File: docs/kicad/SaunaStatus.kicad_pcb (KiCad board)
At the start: 2 copper layers, 9 parts, among them J1 PT1000-Connector, J2 28BYJ-48, J3 28BYJ-48, U1 ESP32-WROOM-32, U2 MAX31865xAP, U3 DHT21/AM2301, U4 DHT21/AM2301, U5 ULN2003A, U6 ULN2003A

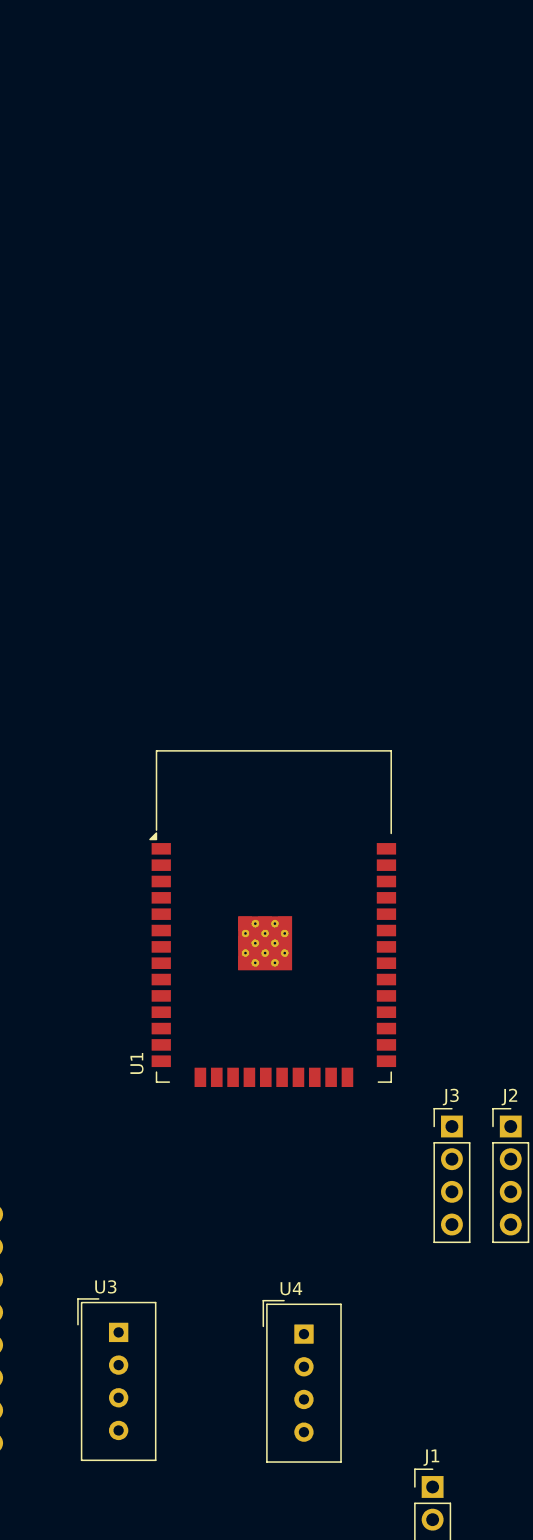
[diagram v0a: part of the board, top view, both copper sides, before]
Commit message: feat(kicad): replace DHT21 sensor footprints with J4/J5 connectors
Sensors are external packages; replace U3/U4 (wrong Sensor:DHT11
footprint) with Conn_01x04 connectors matching AM2301 pinout directly:
Pin1=VDD, Pin2=DATA, Pin3=NC, Pin4=GND.

Also wire INA260 (U7): I2C_SDA/SCL to ESP32 IO4/IO13, VS→+3V3, GND,
A0/A1→GND (address 0x40), VBUS→IN+, INA_IN+/- labels for sense path.

Update PCB footprints, CLAUDE.md, and docs/pinout.md accordingly.

Co-Authored-By: Claude Sonnet 4.6 <noreply@anthropic.com>
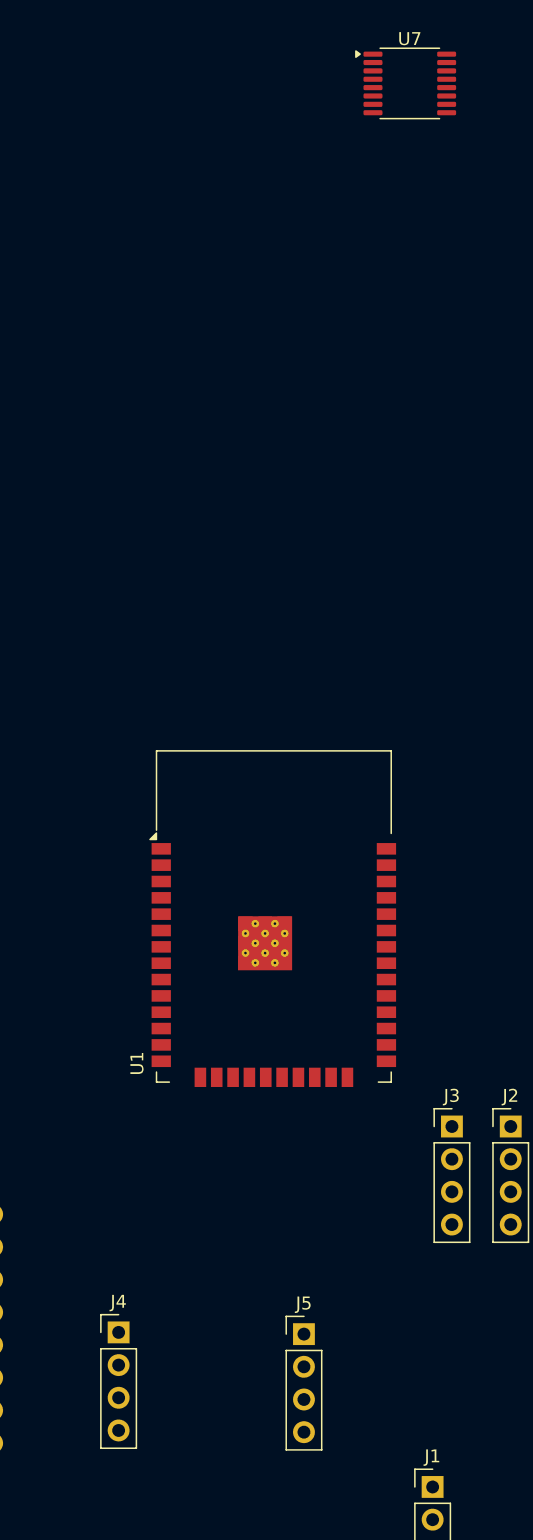
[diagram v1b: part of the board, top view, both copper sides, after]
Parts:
- removed U3, U4: DHT21/AM2301, Sensor:Aosong_DHT11_5.5x12.0_P2.54mm
- added J4: DHT21/AM2301 Ceiling, Connector_PinHeader_2.54mm:PinHeader_1x04_P2.54mm_Vertical, F.Cu at (127.1, 97.3)
- added J5: DHT21/AM2301 Bench, Connector_PinHeader_2.54mm:PinHeader_1x04_P2.54mm_Vertical, F.Cu at (141.5, 97.4)
- added U7: INA260, Package_SO:TSSOP-16_4.4x5mm_P0.65mm, F.Cu at (149.7, 0.23)
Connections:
- U1 pad 16: unconnected-(U1-IO13-Pad16) -> /I2C_SCL
- U1 pad 26: unconnected-(U1-IO4-Pad26) -> /I2C_SDA

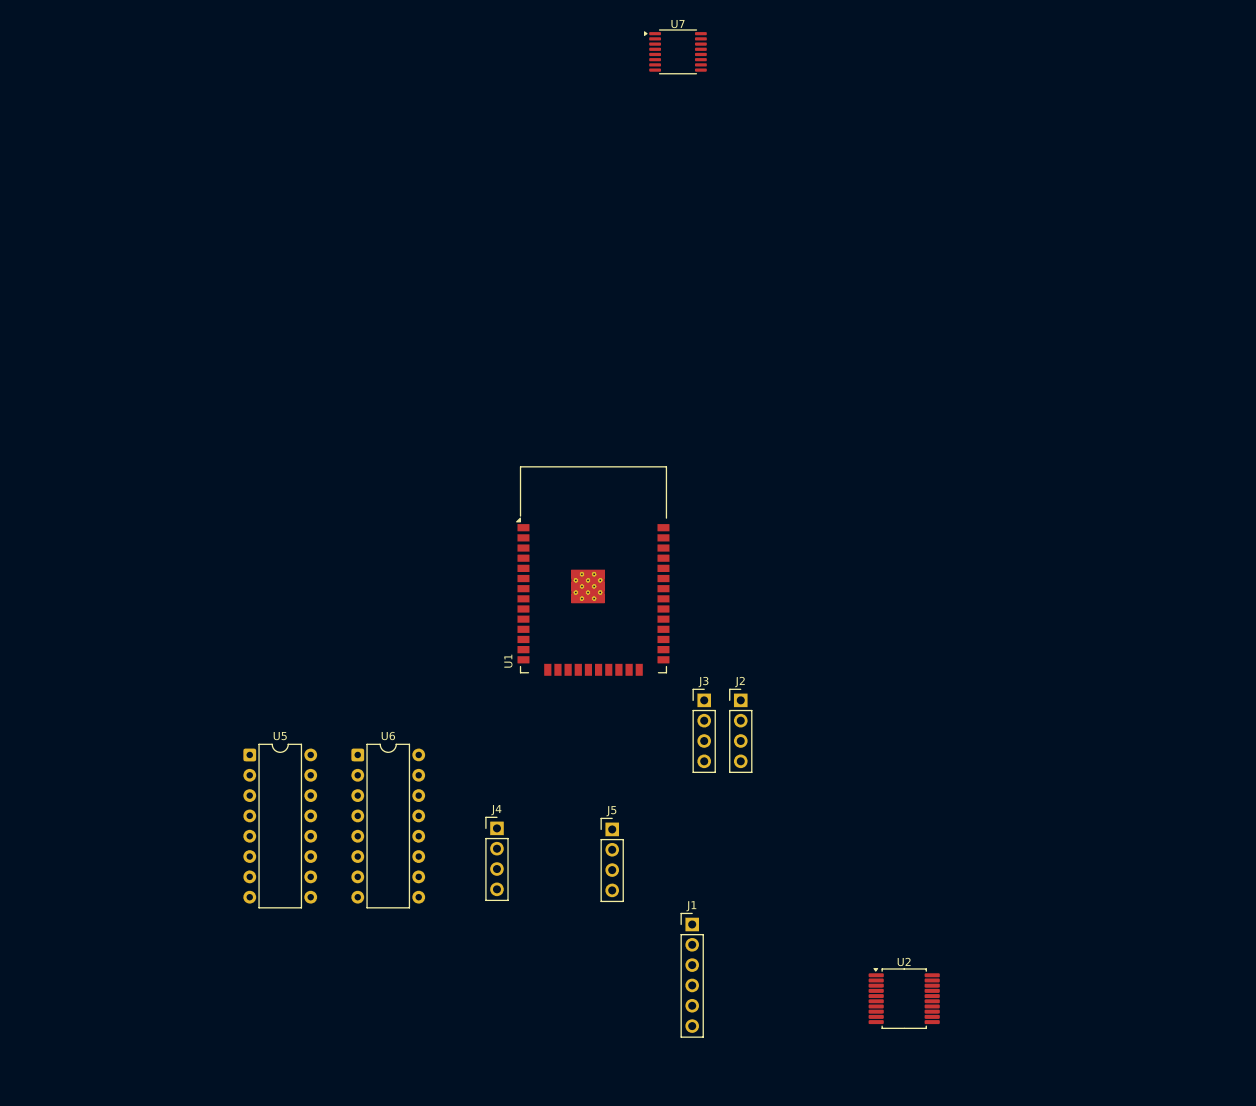
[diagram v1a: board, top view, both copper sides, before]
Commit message: fix(kicad): resolve ERC/DRC errors — wire J4/J5 power pins, U6 outputs, add board outline
ERC fixes (16 errors → expected 4 or fewer):
- J4 (DHT Ceiling connector): add +3V3→Pin1 and Pin4→GND wires
- J5 (DHT Bench connector): add +3V3→Pin1 and Pin4→GND wires
- Remove two dangling data-stub wires left from DHT21→connector replacement
- U6 O1/O2: add wires (162.56→182.88mm) connecting Pin16/15 to J3 Pin1/2
  via U6_28BYJ_A/B labels — mirrors the working C/D pattern

DRC fix:
- Add Edge.Cuts board outline (gr_rect 67,55 → 220,130mm) — no outline existed

Remaining DRC items require KiCad GUI:
- 49 unconnected pads: PCB has 0 routed traces, full layout required
- SSOP-20 (MAX31865) clearance violations: inherent to 0.65mm pitch, use local override
- ESP32 thermal pad 0.2mm vias: violate 0.3mm default min-drill; select fab supporting micro-vias
- Library footprint mismatches: warnings only, accept or re-sync from library

gitignore: add docs/kicad/*.rpt (ERC/DRC reports are generated, not source-controlled)

Co-Authored-By: Claude Sonnet 4.6 <noreply@anthropic.com>
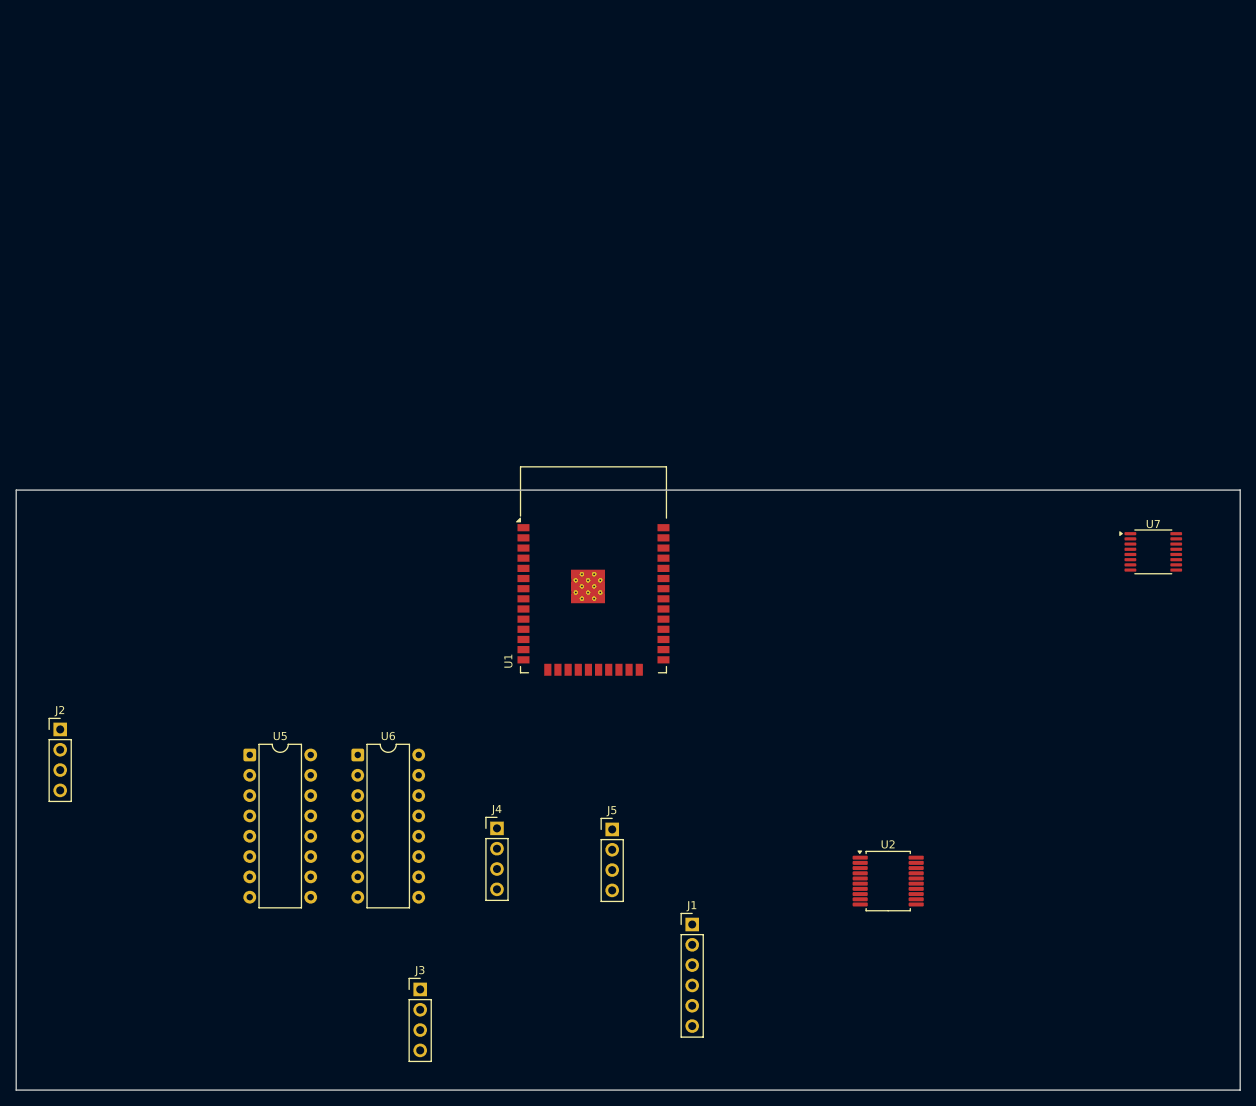
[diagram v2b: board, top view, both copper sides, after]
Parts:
- moved U7 86.2 mm to (209.1, 62.7)
- moved J2 85.1 mm to (72.5, 84.9)
- moved J3 50.7 mm to (117.5, 117.4)
- moved U2 14.8 mm to (176.0, 103.9)
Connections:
- J3 pad 1: /U6_28BYJ_A -> unconnected-(J3-Pin_1-Pad1)
- J3 pad 2: /U6_28BYJ_B -> unconnected-(J3-Pin_2-Pad2)
- J4 pad 1: +3V3 -> unconnected-(J4-Pin_1-Pad1)
- J4 pad 3: (no net) -> unconnected-(J4-Pin_3-Pad3)
- J4 pad 4: GND -> unconnected-(J4-Pin_4-Pad4)
- J5 pad 1: +3V3 -> unconnected-(J5-Pin_1-Pad1)
- J5 pad 3: (no net) -> unconnected-(J5-Pin_3-Pad3)
- J5 pad 4: GND -> unconnected-(J5-Pin_4-Pad4)
- U6 pad 15: /U6_28BYJ_B -> unconnected-(U6-O2-Pad15)
- U6 pad 16: /U6_28BYJ_A -> unconnected-(U6-O1-Pad16)
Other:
- board outline added: 153 x 75 mm

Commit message: feat(board): change board from denky32 to esp32doit-devkit-v1
Physical chip is ESP32-D0WD-V3 (revision v3.1) on an ESP32-WROOM-32
dev board — the correct PlatformIO definition is esp32doit-devkit-v1,
not denky32 (a CH2i energy meter board).

Removes three incorrect PSRAM build flags and corrects flash frequency
from 80 MHz to 40 MHz (WROOM-32 spec). All 16 project GPIOs are
pin-compatible between the two board definitions; no firmware changes
required. All 113 unit tests pass. Build verified with pio run.

Co-Authored-By: Claude Sonnet 4.6 <noreply@anthropic.com>
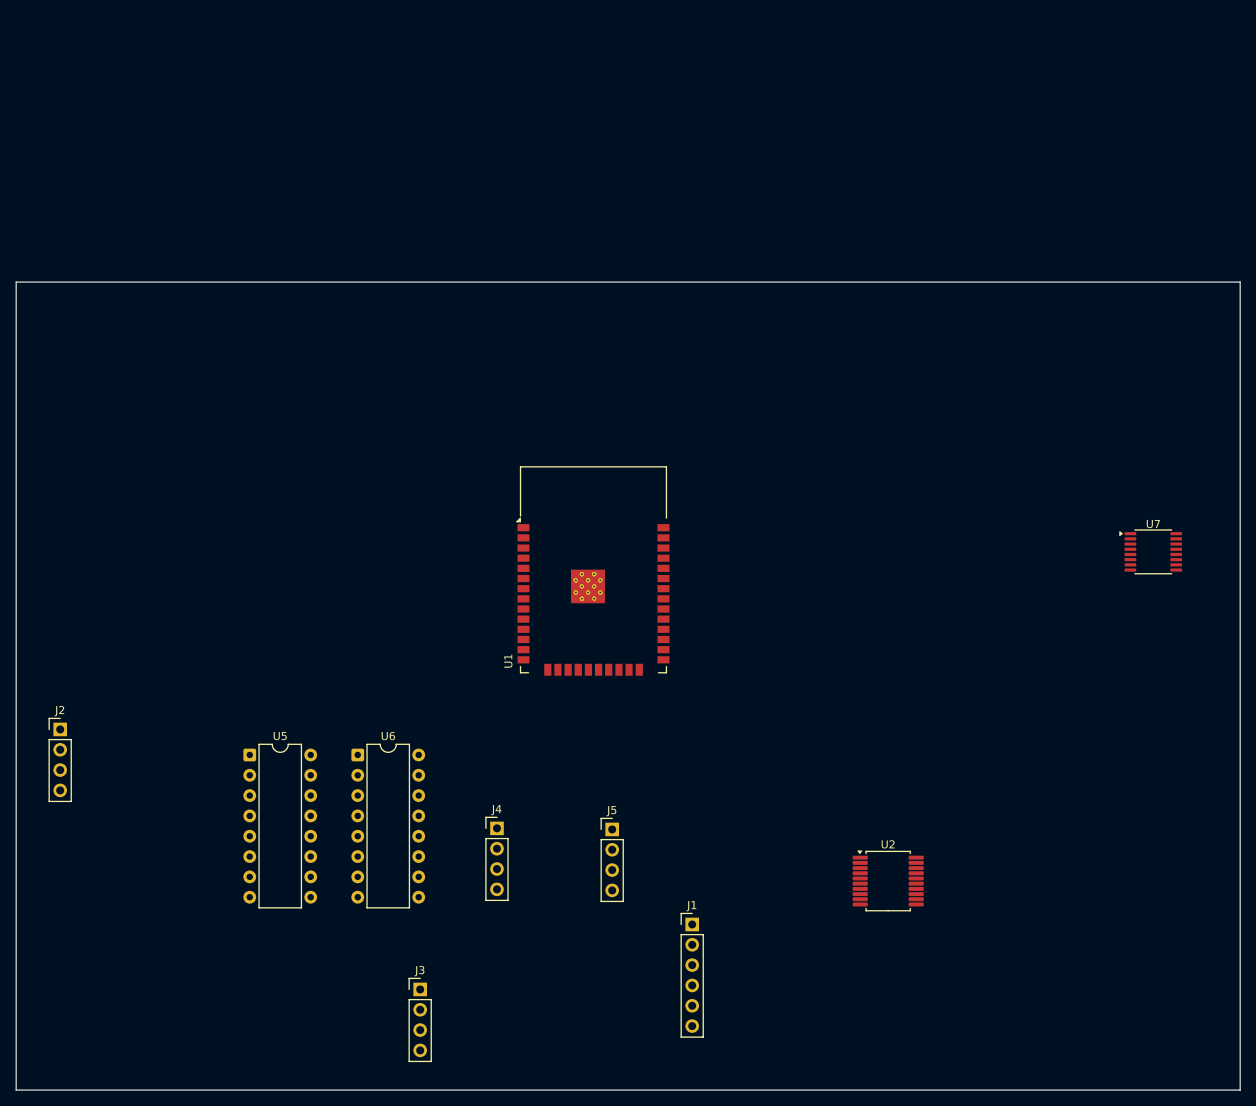
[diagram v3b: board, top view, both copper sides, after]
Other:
- board size 153 x 75 mm -> 153 x 101 mm
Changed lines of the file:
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@@
 	)
 	(gr_rect
-		(start 67 55)
+		(start 67 29)
 		(end 220 130)
 		(stroke
@@
 			(type default)
 		)
-		(fill none)
+		(fill no)
 		(layer "Edge.Cuts")
-		(uuid "edge0001-0000-0000-0000-000000000001")
 	)
 	(embedded_fonts no)

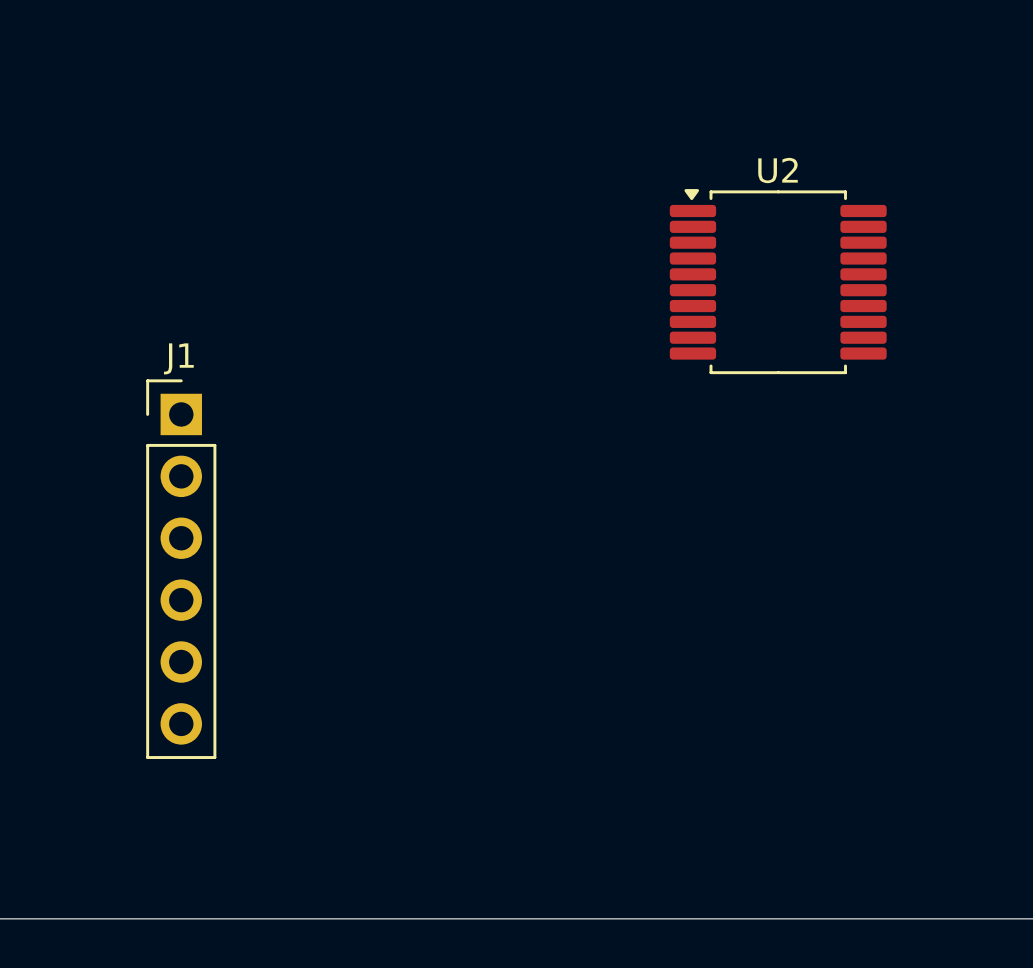
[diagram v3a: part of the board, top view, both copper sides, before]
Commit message: feat(kicad): replace MAX31865 bare IC with Adafruit breakout connector
Remove U2 (MAX31865xAP SSOP-20) and J1 (6-pin PT1000 connector);
replace with J1 (Conn_01x08) for Adafruit MAX31865 breakout board.
SPI GPIO assignments unchanged (CS=5, SCK=18, MISO=19, MOSI=23).

Pin mapping on new J1:
  1=VIN(+3V3)  2=3Vo(NC)  3=GND  4=CLK(SPI_SCK)
  5=SDO(SPI_MISO)  6=SDI(SPI_MOSI)  7=CS(SPI_CS)  8=RDY(NC)

Remove 6 stale RTD net declarations from PCB (RTDIN+/-, FORCE+/-,
REFIN+/-). DRC improved from 34 to 16 violations (all pre-existing).
All 113 native unit tests pass.

Hardware prerequisite: set Adafruit breakout 3-wire solder jumper
before installation (ships in 2-wire/4-wire mode by default).

Co-Authored-By: Claude Sonnet 4.6 <noreply@anthropic.com>
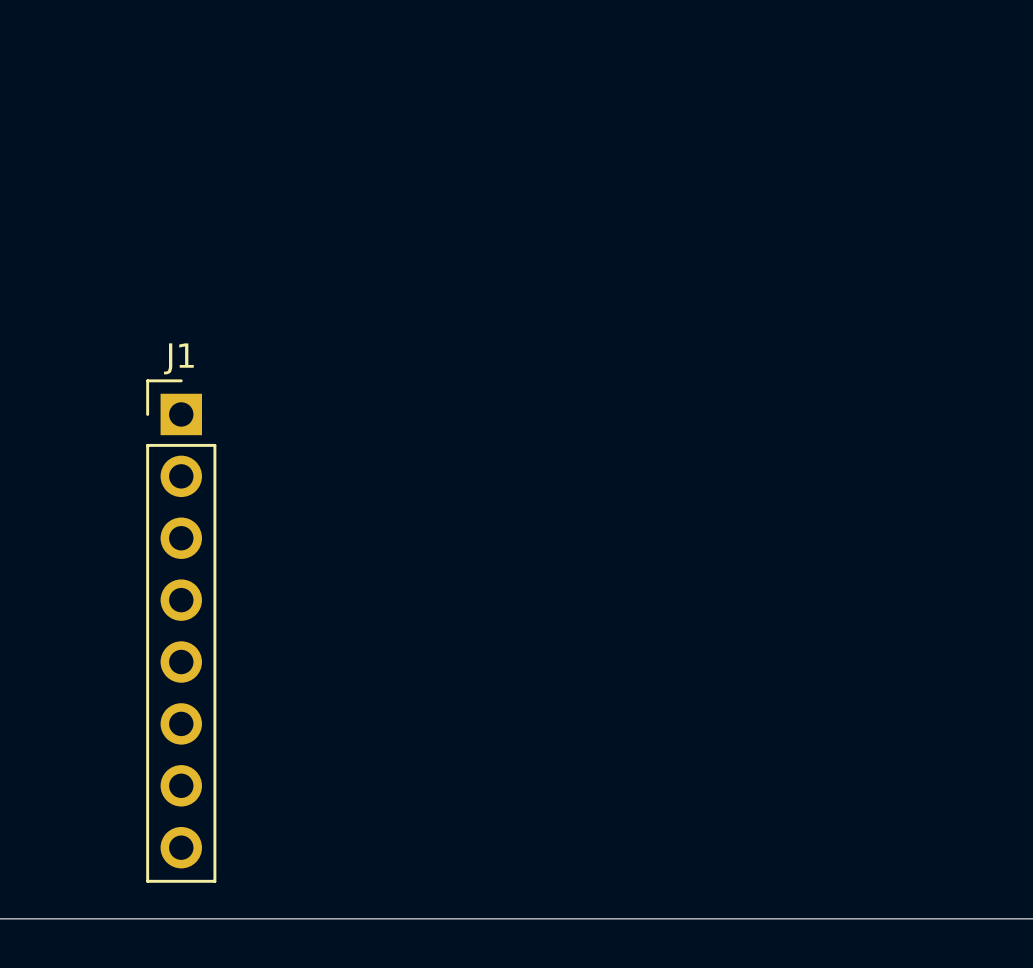
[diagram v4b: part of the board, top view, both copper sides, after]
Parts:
- removed U2: MAX31865xAP, Package_SO:SSOP-20_5.3x7.2mm_P0.65mm
- J1: value PT1000-Connector -> Adafruit-MAX31865-Breakout; footprint Connector_PinHeader_2.54mm:PinHeader_1x06_P2.54mm_Vertical -> PinHeader_1x08_P2.54mm_Vertical
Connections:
- J1 pad 1: /REFIN+ -> (no net)
- J1 pad 2: /FORCE+ -> (no net)
- J1 pad 3: /RTDIN+ -> (no net)
- J1 pad 4: /RTDIN- -> (no net)
- J1 pad 5: /FORCE- -> (no net)
- J1 pad 6: /REFIN- -> (no net)
